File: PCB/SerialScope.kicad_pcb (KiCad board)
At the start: 2 copper layers, 220 x 100 mm, 61 parts, among them J1 Conn_01x15, J2 Conn_01x15, J3 Conn_01x15, J4 Conn_01x15, J5 Conn_01x15, J6 Conn_01x15

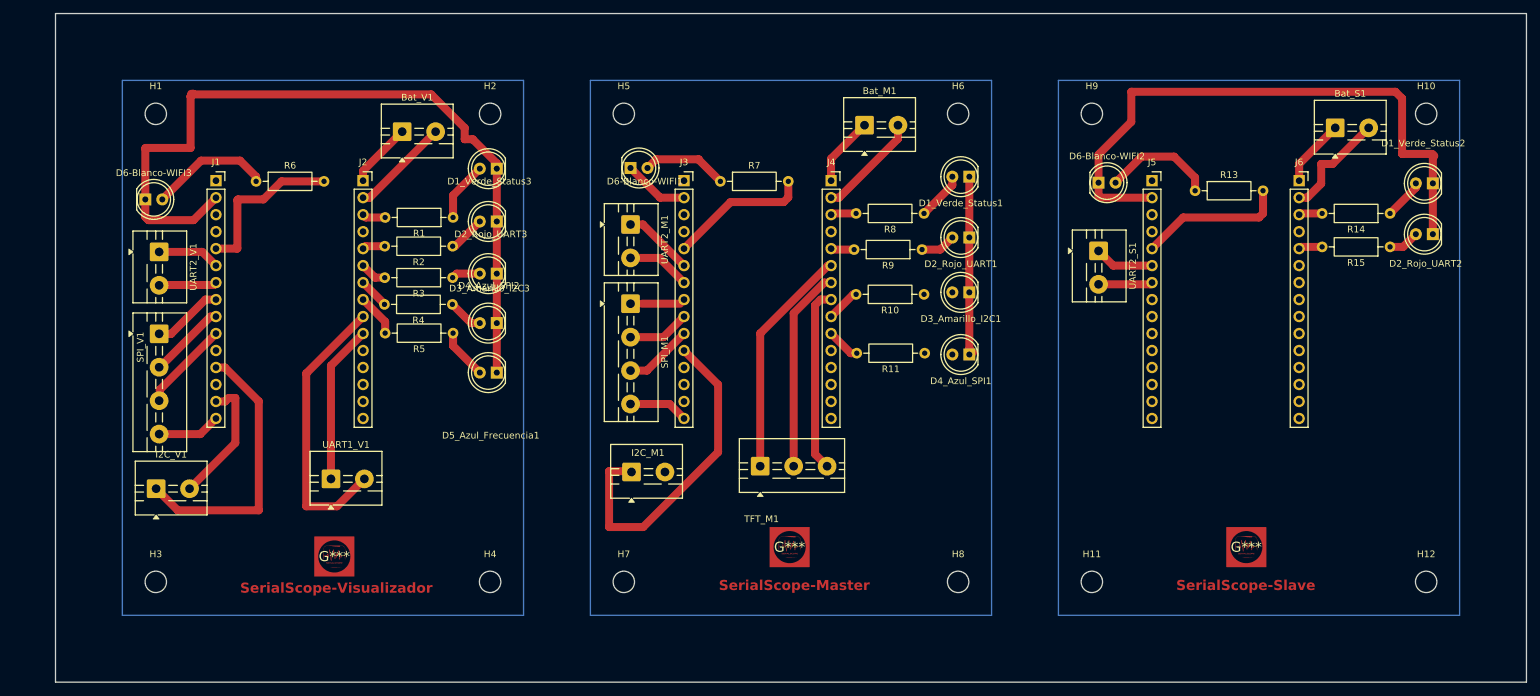
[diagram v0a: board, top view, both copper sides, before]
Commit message: Modificacion pcb , 2 mm extras de separacion entre las hileras de pines para esp32
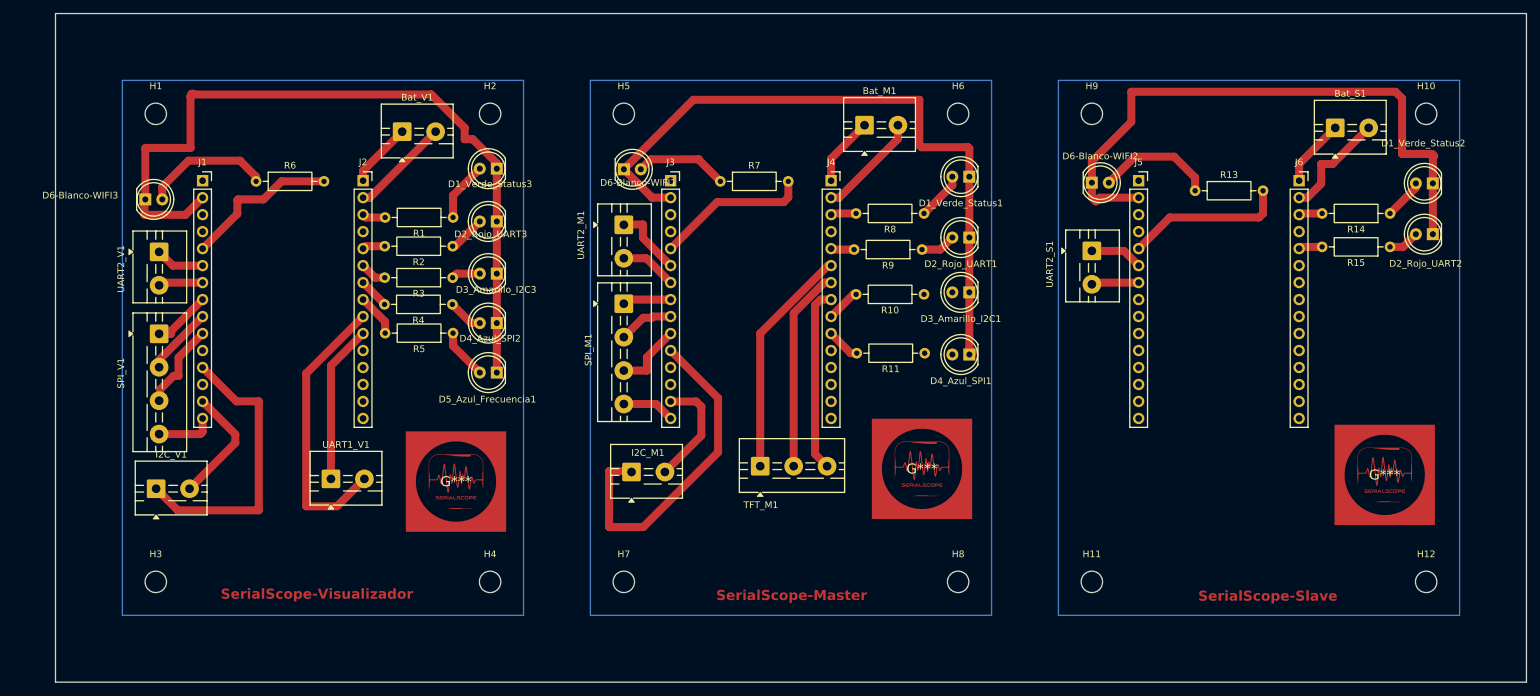
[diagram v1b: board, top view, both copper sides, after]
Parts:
- removed the G*** at (41.7, 81.2)
- removed the G*** at (109.8, 79.8)
- removed the G*** at (178.1, 79.8)
- added G***: LOGO, SerialScope:Logo_15x15, F.Cu at (129.6, 68.1)
- added G***: LOGO, SerialScope:Logo_15x15, F.Cu at (59.9, 70.0)
- added G***: LOGO, SerialScope:Logo_15x15, F.Cu at (198.8, 69.0)
- moved J1 2.00 mm to (22.0, 25.0)
- moved J3 2.00 mm to (92.0, 25.0)
- moved J5 2.00 mm to (162.0, 25.0)
- moved D6-Blanco-WIFI1 1.02 mm to (85.0, 23.3)
- moved UART2_M1 1.00 mm to (85.0, 31.6)
- moved D6-Blanco-WIFI2 1.00 mm to (155.0, 25.3)
- moved SPI_M1 1.00 mm to (85.0, 43.4)
- moved UART2_S1 1.00 mm to (155.0, 35.5)
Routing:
- net Net-(D1_Verde_Status1-K): track 36.4 -> 102.5 mm
- net Net-(I2C_M1-Pin_2): track 0.00 -> 16.9 mm
- net Net-(D1_Verde_Status3-K): track 120.3 -> 117.6 mm
- net Net-(J5-Pin_5): track 22.2 -> 24.2 mm
- net Net-(J3-Pin_5): track 21.2 -> 23.2 mm
- net Net-(I2C_V1-Pin_1): track 41.5 -> 43.5 mm
- net Net-(J1-Pin_6): track 9.22 -> 7.35 mm
- net Net-(J1-Pin_7): track 8.47 -> 6.67 mm
- net Net-(J1-Pin_8): track 10.5 -> 8.77 mm
- net Net-(I2C_V1-Pin_2): track 19.5 -> 17.9 mm
- net Net-(J3-Pin_8): track 5.72 -> 7.26 mm
- net Net-(J1-Pin_9): track 11.5 -> 10.3 mm
- net Net-(D6-Blanco-WIFI3-A): track 18.1 -> 19.2 mm
- net Net-(D6-Blanco-WIFI1-A): track 12.8 -> 13.9 mm
- net Net-(J1-Pin_5): track 24.6 -> 23.5 mm
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
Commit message: Actualizacion medidas , correcciones de medidas
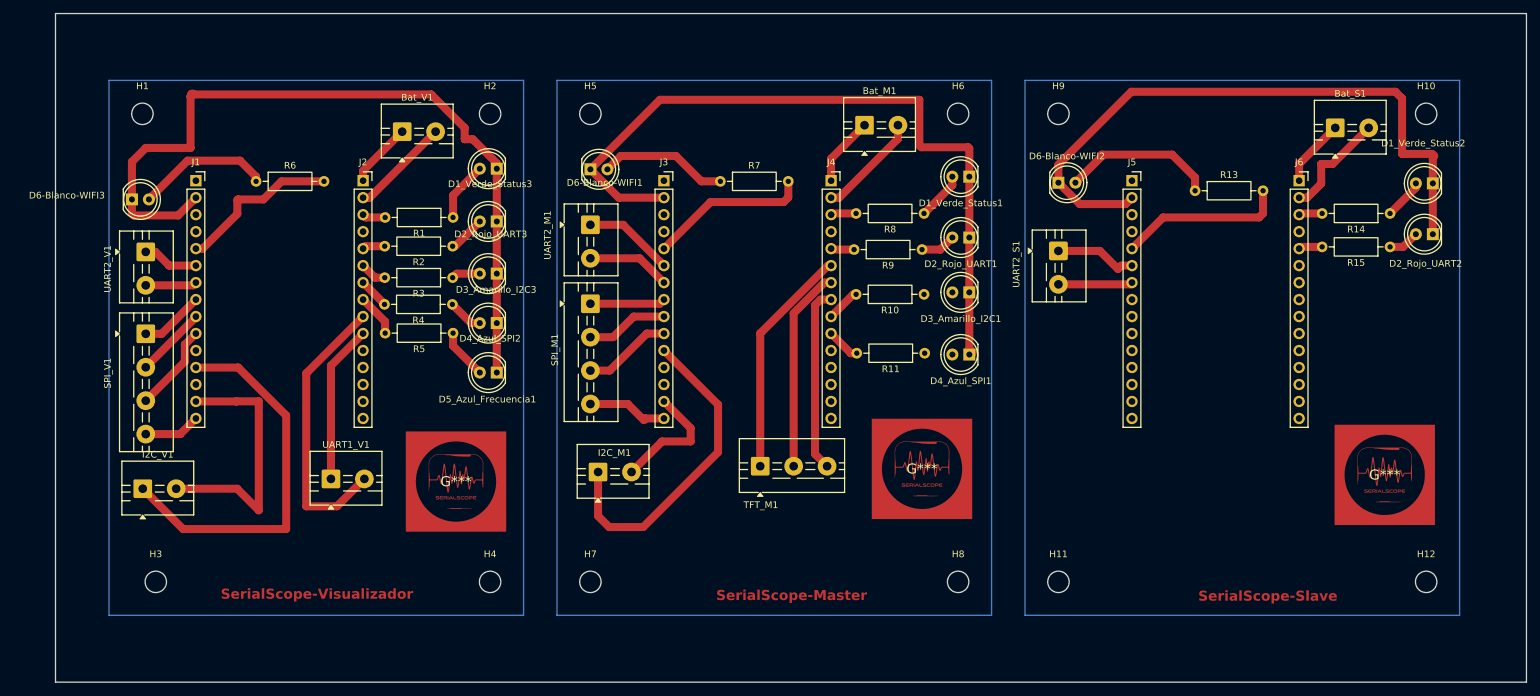
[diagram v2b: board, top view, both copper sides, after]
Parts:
- moved D6-Blanco-WIFI1 5.00 mm to (80.0, 23.3)
- moved D6-Blanco-WIFI2 5.00 mm to (150.0, 25.3)
- moved H11 5.00 mm to (150.0, 85.0)
- moved H5 5.00 mm to (80.0, 15.0)
- moved H7 5.00 mm to (80.0, 85.0)
- moved H9 5.00 mm to (150.0, 15.0)
- moved I2C_M1 5.00 mm to (81.2, 68.6)
- moved SPI_M1 5.00 mm to (80.0, 43.4)
- moved UART2_M1 5.00 mm to (80.0, 31.6)
- moved UART2_S1 5.00 mm to (150.0, 35.5)
- moved D6-Blanco-WIFI3 2.00 mm to (11.4, 27.8)
- moved H1 2.00 mm to (13.0, 15.0)
- moved I2C_V1 2.00 mm to (13.1, 71.1)
- moved SPI_V1 2.00 mm to (13.5, 47.9)
- moved UART2_V1 2.00 mm to (13.5, 35.6)
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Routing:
- net Net-(I2C_V1-Pin_2): track 17.9 -> 39.4 mm
- net Net-(I2C_V1-Pin_1): track 43.5 -> 57.4 mm
- net Net-(D1_Verde_Status1-K): track 102.5 -> 111.5 mm
- net Net-(D6-Blanco-WIFI2-A): track 17.8 -> 23.2 mm
- net Net-(D6-Blanco-WIFI1-A): track 13.9 -> 19.3 mm
- net Net-(D1_Verde_Status2-K): track 91.6 -> 96.8 mm
- net Net-(J5-Pin_6): track 7.91 -> 12.3 mm
- net Net-(J3-Pin_15): track 7.89 -> 12.1 mm
- net Net-(J5-Pin_7): track 7.11 -> 11.1 mm
- net Net-(J3-Pin_8): track 7.26 -> 11.3 mm
- net Net-(J3-Pin_7): track 8.51 -> 12.5 mm
- net Net-(J3-Pin_9): track 8.28 -> 12.3 mm
- net Net-(J3-Pin_10): track 9.47 -> 13.3 mm
- net Net-(J3-Pin_6): track 9.72 -> 13.5 mm
- net Net-(I2C_M1-Pin_1): track 50.6 -> 48.4 mm
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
